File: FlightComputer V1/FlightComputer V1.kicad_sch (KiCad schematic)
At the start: 0 parts

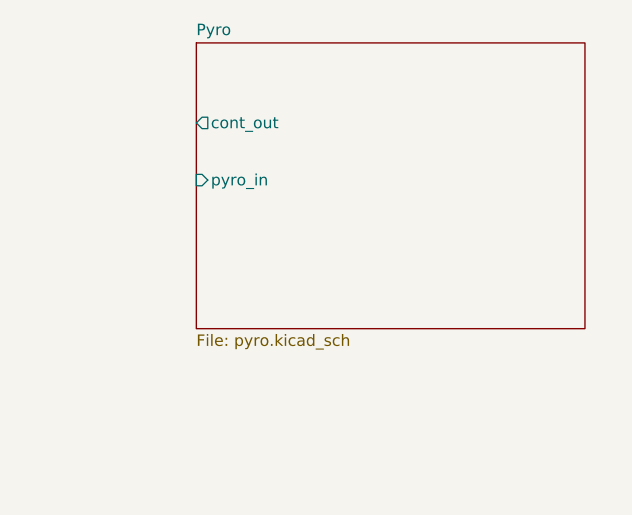
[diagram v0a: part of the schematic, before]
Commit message: Update pyro channel. Duplicate sheet. Paramatarize labels
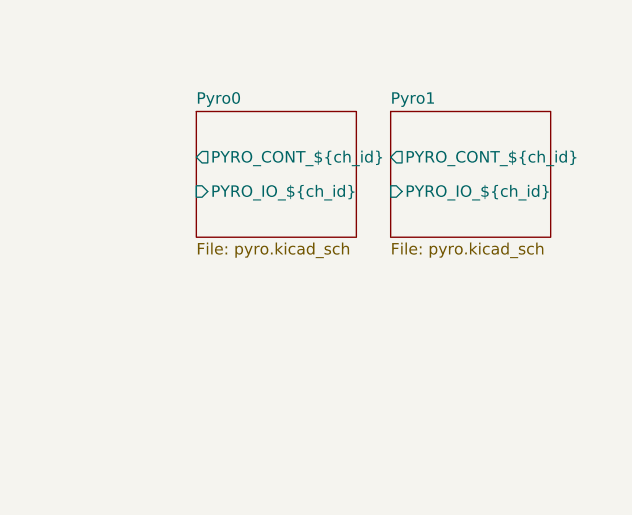
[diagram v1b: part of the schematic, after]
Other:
- sheet Pyro renamed Pyro0
- added sheet Pyro1 (pyro.kicad_sch)
- sheet Pyro0 ports: added PYRO_CONT_${ch_id}, PYRO_IO_${ch_id}; removed cont_out, pyro_in
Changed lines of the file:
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@@
 	(paper "A4")
+	(sheet
+		(at 186.69 77.47)
+		(size 17.78 13.97)
+		(exclude_from_sim no)
+		(in_bom yes)
+		(on_board yes)
+		(dnp no)
+		(fields_autoplaced yes)
+		(stroke
+			(width 0.1524)
+			(type solid)
+		)
+		(fill
+			(color 0 0 0 0.0000)
+		)
+		(property "Sheetname" "Pyro1"
+			(at 186.69 76.7584 0)
+			(effects
+				(font
+					(size 1.27 1.27)
+				)
+				(justify left bottom)
+			)
+		)
+		(property "Sheetfile" "pyro.kicad_sch"
+			(at 186.69 92.0246 0)
+			(effects
+				(font
+					(size 1.27 1.27)
+				)
+				(justify left top)
+			)
+		)
+		(property "ch_id" "1"
+			(at 186.69 77.47 0)
+			(effects
+				(font
+					(size 1.27 1.27)
+				)
+				(hide yes)
+			)
+		)
+		(pin "PYRO_CONT_${ch_id}" output
+			(at 186.69 82.55 180)
+			(effects
+				(font
+					(size 1.27 1.27)
+				)
+				(justify left)
+			)
+		)
+		(pin "PYRO_IO_${ch_id}" input
+			(at 186.69 86.36 180)
+			(effects
+				(font
+					(size 1.27 1.27)
+				)
+				(justify left)
+			)
+		)
+		(instances
+			(project "FlightComputer V1"
+				(path "/9c0e1766-b875-44c2-9c31-cf47efaf79e2"
+					(page "5")
+				)
+			)
+		)
+	)
 	(sheet
 		(at 88.9 115.57)
@@
 	)
 	(sheet
-		(at 165.1 69.85)
-		(size 43.18 31.75)
+		(at 165.1 77.47)
+		(size 17.78 13.97)
 		(exclude_from_sim no)
 		(in_bom yes)
@@
 			(color 0 0 0 0.0000)
 		)
-		(property "Sheetname" "Pyro"
-			(at 165.1 69.1384 0)
+		(property "Sheetname" "Pyro0"
+			(at 165.1 76.7584 0)
 			(effects
 				(font
@@
 		)
 		(property "Sheetfile" "pyro.kicad_sch"
-			(at 165.1 102.1846 0)
+			(at 165.1 92.0246 0)
 			(effects
 				(font
@@
 			)
 		)
-		(pin "cont_out" output
-			(at 165.1 78.74 180)
+		(property "ch_id" "0"
+			(at 165.1 77.47 0)
+			(effects
+				(font
+					(size 1.27 1.27)
+				)
+				(hide yes)
+			)
+		)
+		(pin "PYRO_CONT_${ch_id}" output
+			(at 165.1 82.55 180)
 			(effects
 				(font
@@
 			)
 		)
-		(pin "pyro_in" input
-			(at 165.1 85.09 180)
+		(pin "PYRO_IO_${ch_id}" input
+			(at 165.1 86.36 180)
 			(effects
 				(font
